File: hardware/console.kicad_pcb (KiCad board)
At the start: 2 copper layers, 56 parts, among them J1 USB-C_Module, J3 SWD, J4 UART, J5 LiPo_140mAh, SW1 SW_LEFT, SW10 SW_BOOT0, SW2 SW_RIGHT, SW3 SW_UP, SW4 SW_DOWN, SW5 SW_A, SW6 SW_B, SW7 SW_POWER, SW8 SW_START, SW9 SW_SELECT, U1 STM32G0B1CBT6, U2 XC6206P332MR, U3 TP4054

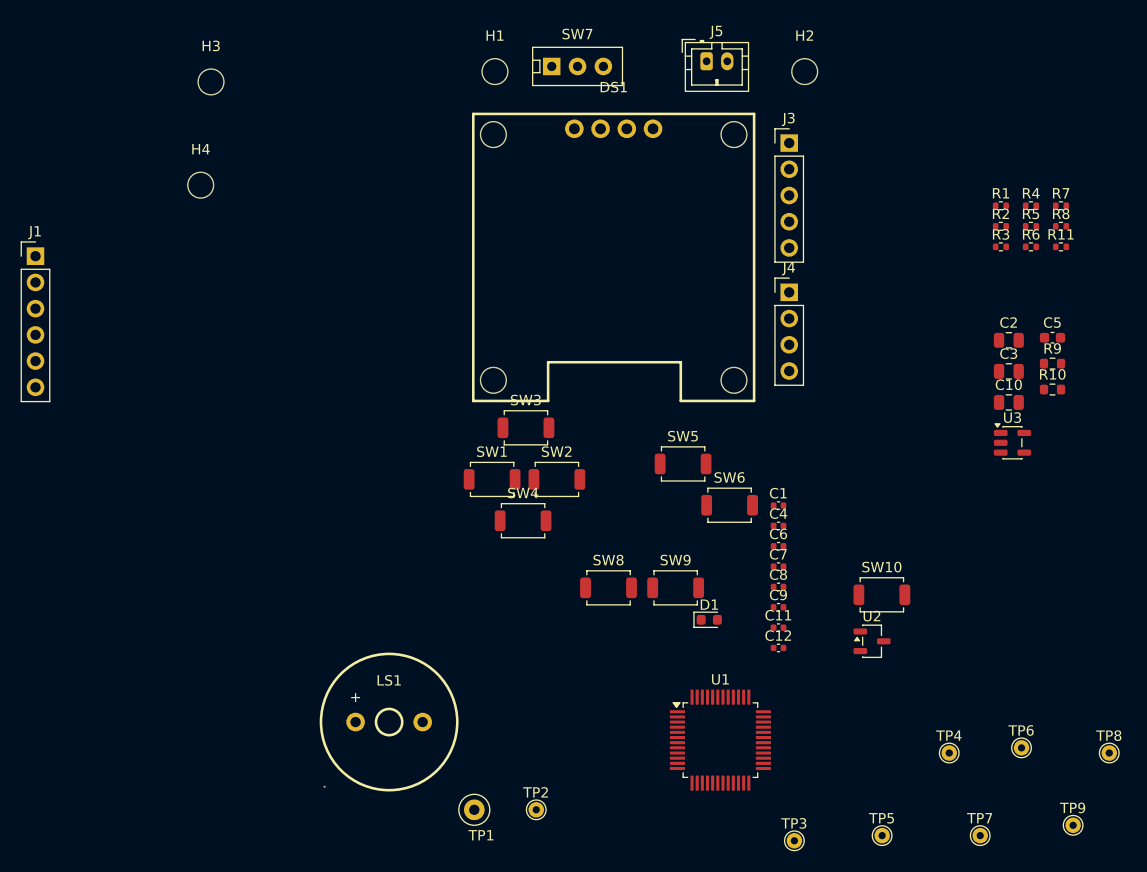
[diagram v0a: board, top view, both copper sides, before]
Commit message: footprint for usb module, and a AI-generated 3d model
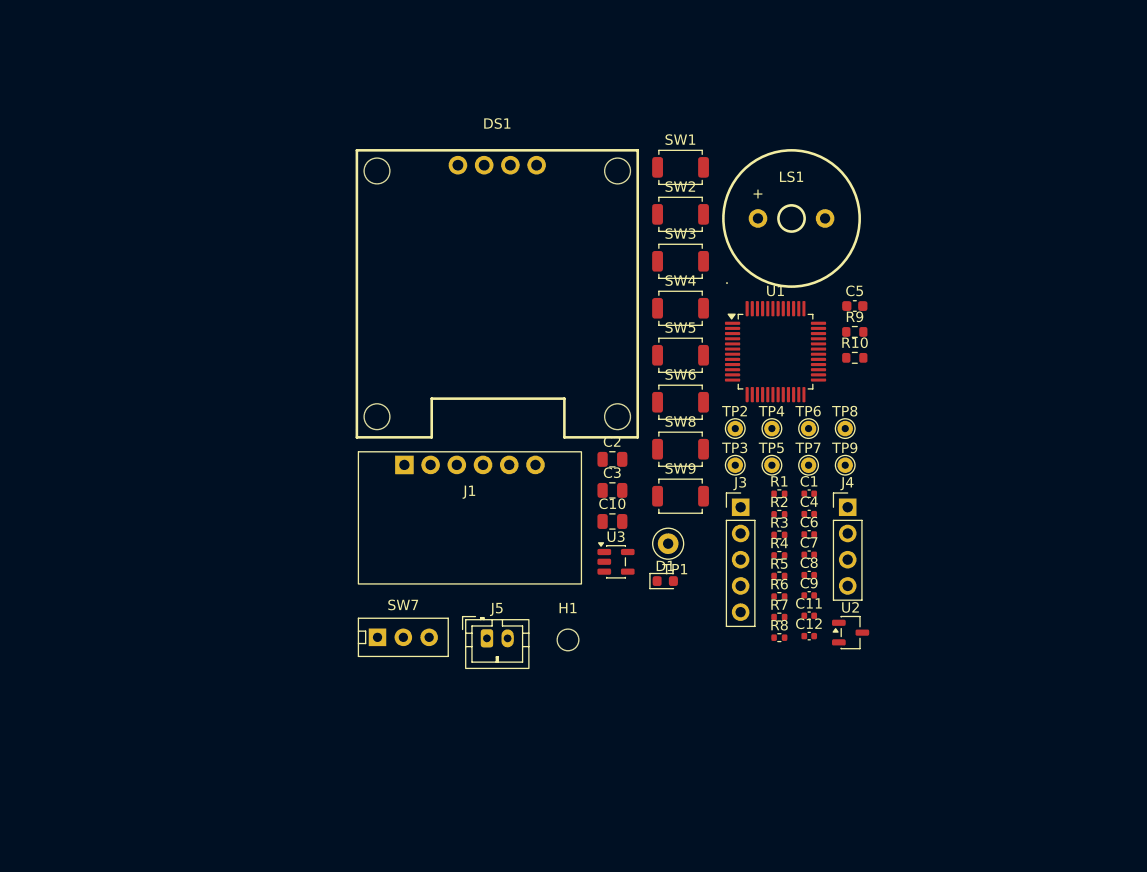
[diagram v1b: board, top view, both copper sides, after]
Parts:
- removed H2, H3, H4: MountingHole, MountingHole:MountingHole_2.5mm
- removed R11: 10k, Resistor_SMD:R_0402_1005Metric
- removed SW10: SW_BOOT0, Button_Switch_SMD:SW_SPST_TS-1088-xR020
- H1: footprint MountingHole:MountingHole_2.5mm -> MountingHole:MountingHole_2.1mm
- J1: footprint Connector_PinHeader_2.54mm:PinHeader_1x06_P2.54mm_Vertical -> console:USBC-TH_L21.6-W12.8-P2.54
- moved LS1 62.4 mm to (107.2, 48.7)
- moved J5 59.8 mm to (77.7, 89.4)
- moved SW7 57.8 mm to (69.6, 89.3)
- moved H1 55.5 mm to (85.6, 89.5)
- moved R8 48.3 mm to (106.0, 89.3)
- moved R7 48.3 mm to (106.0, 87.3)
- moved J1 46.7 mm to (76.1, 72.6)
- moved R5 41.7 mm to (106.0, 83.4)
- moved R4 41.7 mm to (106.0, 81.4)
- moved R6 41.7 mm to (106.0, 85.3)
- moved TP2 41.7 mm to (101.8, 69.1)
- moved TP9 41.3 mm to (112.4, 72.6)
- moved TP8 40.5 mm to (112.4, 69.1)
- moved C10 40.1 mm to (89.9, 78.1)
- moved C2 40.1 mm to (89.9, 72.1)
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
